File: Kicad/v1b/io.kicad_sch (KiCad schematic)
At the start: 9 parts, among them J1 KeyIN, J2 KeyOUT, U30 74HC138, U31 74HCT540, U32 74HC273

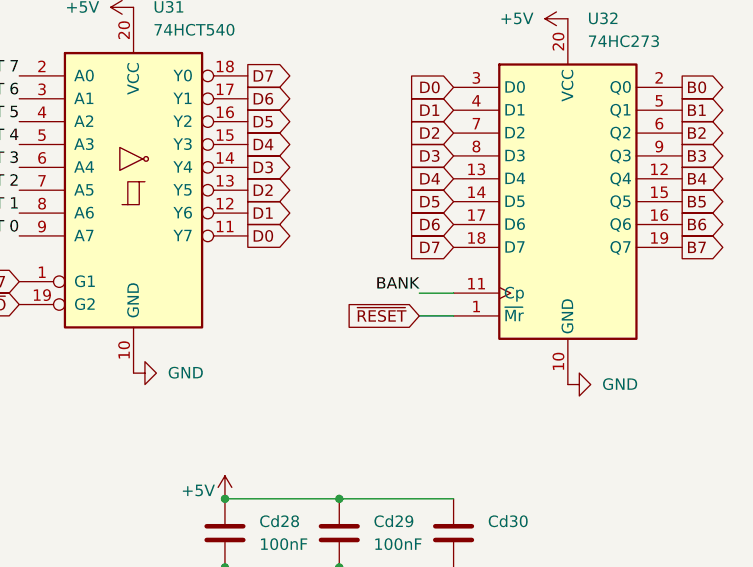
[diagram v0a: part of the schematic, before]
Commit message: Video ROM update, cart files, v1b main board
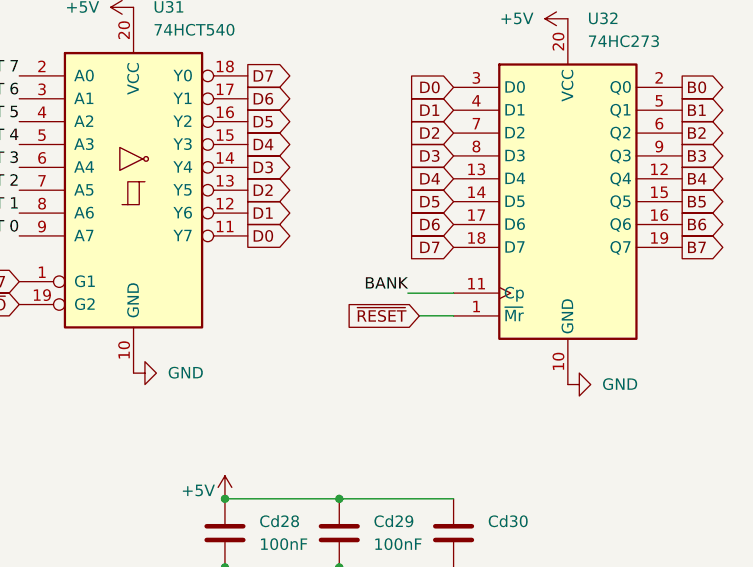
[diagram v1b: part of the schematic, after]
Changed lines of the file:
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@@
     (stroke (width 0) (type default))
   )
-  (wire (pts (xy 157.48 66.04) (xy 161.29 66.04))
+  (wire (pts (xy 156.21 66.04) (xy 161.29 66.04))
     (stroke (width 0) (type default))
   )
@@
     (effects (font (size 1.27 1.27)) (justify right bottom))
   )
-  (label "BANK" (at 157.48 66.04 180) (fields_autoplaced)
+  (label "BANK" (at 156.21 66.04 180) (fields_autoplaced)
     (effects (font (size 1.27 1.27)) (justify right bottom))
   )
